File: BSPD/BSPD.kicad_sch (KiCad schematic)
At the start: 82 parts, among them J1 Conn_01x15_Pin, J2 Conn_01x15_Pin, U1 TLV2371DBV, U10 TLV2371DBV, U13 74LVC1G08, U14 AP2204K-ADJ, U15 AP7375Q-50WR-7, U17 74LVC1G08, U18 74LVC1G08, U2 TLV2371DBV, U3 TLV2371DBV, U4 TLV2371DBV, U8 TLV2371DBV, U9 TLV2371DBV

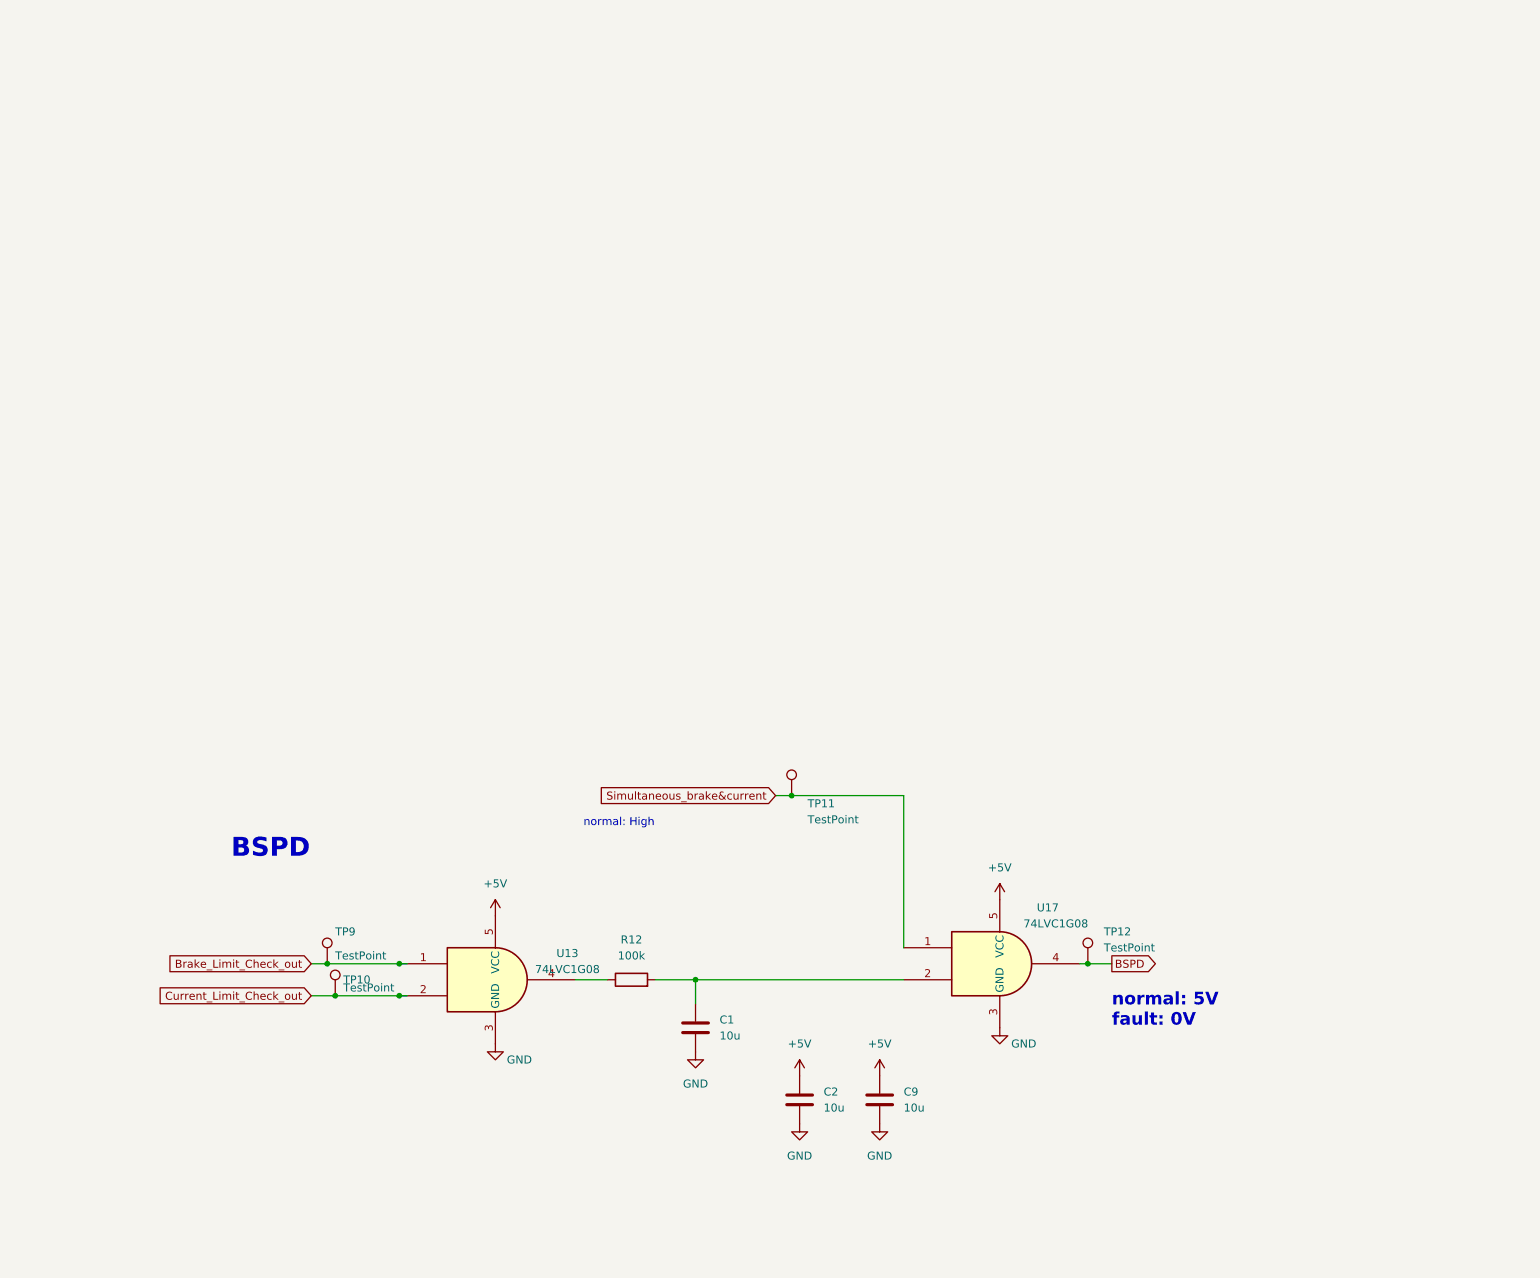
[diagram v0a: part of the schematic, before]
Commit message: BSPD v3 finish basic layout
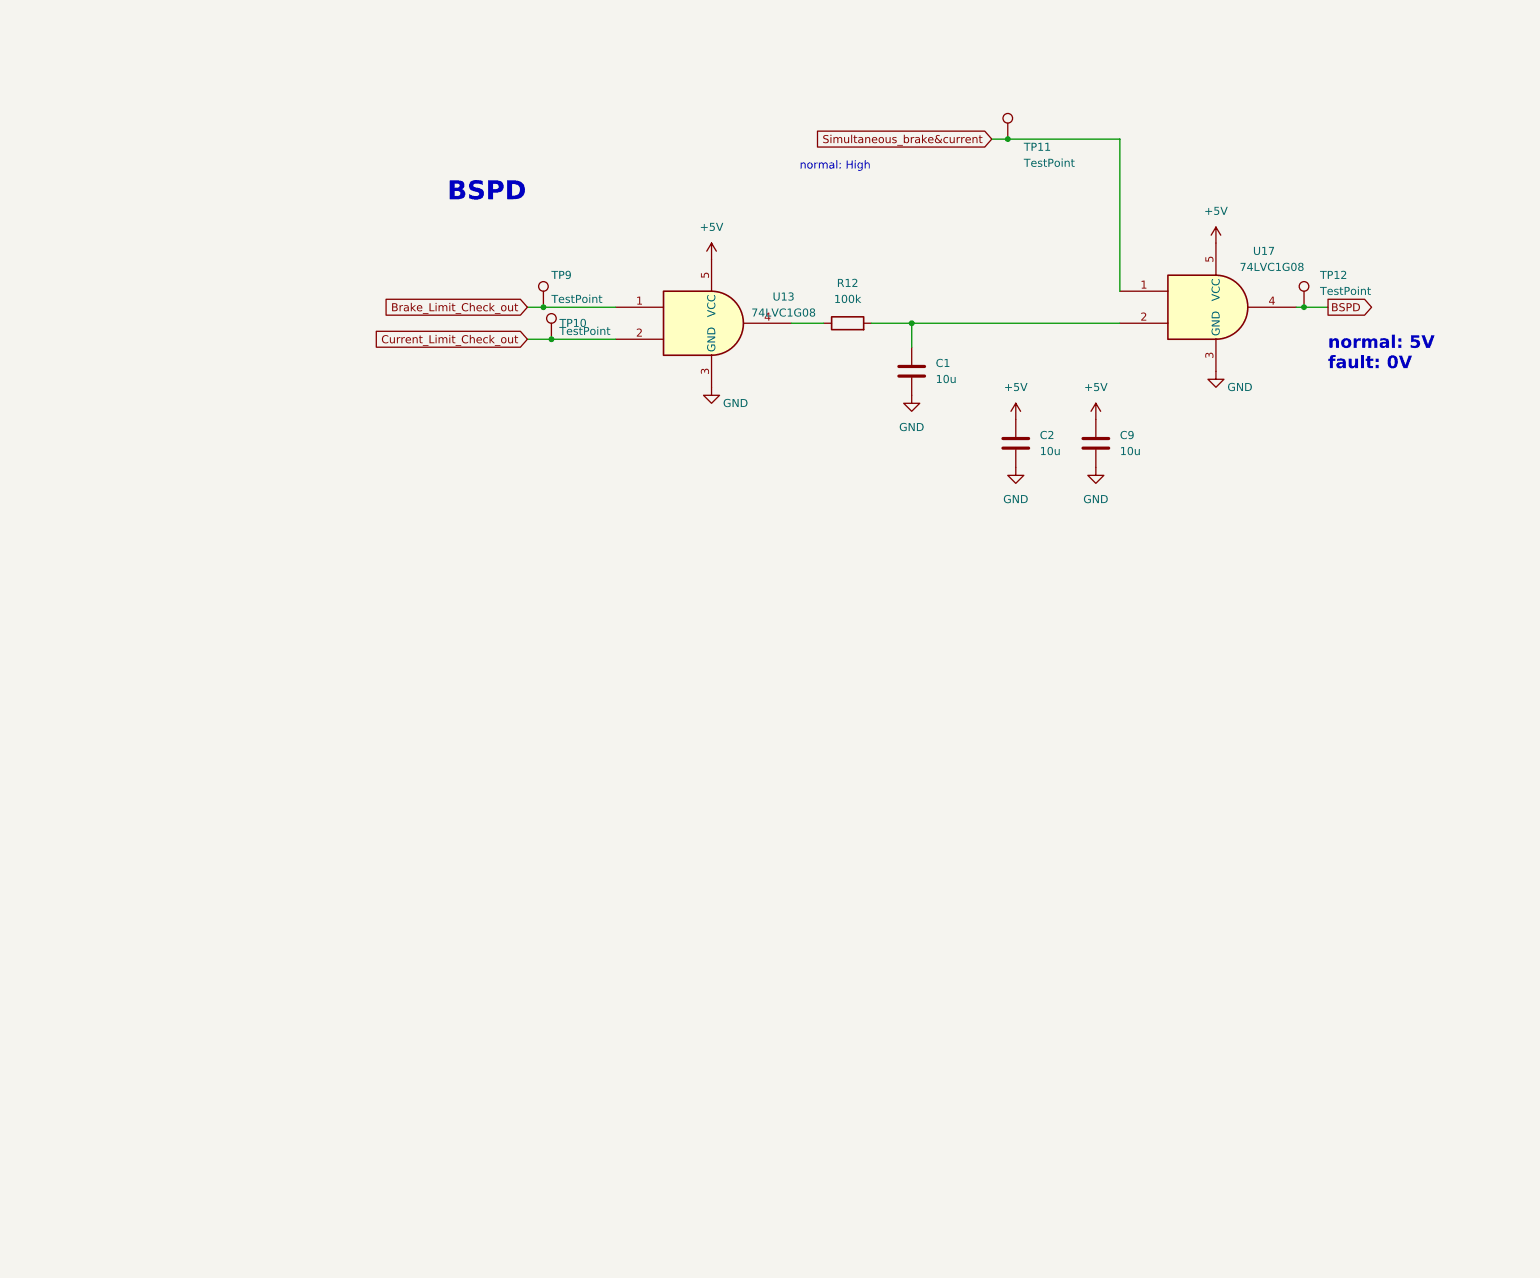
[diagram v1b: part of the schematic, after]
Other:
- moved on the sheet: C1, C2, C9, R12, TP10, TP11, TP12, TP9, U13, U17

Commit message: SDC add pinheader
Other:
- moved on the sheet: C13, C14, C15, C25, C3, C4, C5, D18, D5, D6, D7, R16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

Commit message: Add And gate and R at limit chack
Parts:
- added C6, C7: 10u, Capacitor_SMD:C_0805_2012Metric_Pad1.18x1.45mm_HandSolder, symbol Device:C
- added R11, R13, R7, R9: 10k, Resistor_SMD:R_0603_1608Metric_Pad0.98x0.95mm_HandSolder, symbol Device:R
- added U5, U6: 74LVC1G08, Package_TO_SOT_SMD:SOT-23-5, symbol 74xGxx:74LVC1G08
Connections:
- net +5V: now also C6.1, C7.1, U5.5 (VCC), U6.5 (VCC)
- net Brake_Limit_Check_out: now also U6.4; no longer U3.1, U4.1
- net Current_Limit_Check_out: now also U5.4; no longer U1.1, U2.1
- net GND: now also C6.2, C7.2, U5.3 (GND), U6.3 (GND)
- new net: R7.1, U1.1
- new net: R7.2, U5.1
- new net: R11.1, U3.1
- new net: R11.2, U6.1
- new net: R9.1, U2.1
- new net: R9.2, U5.2
- new net: R13.1, U4.1
- new net: R13.2, U6.2
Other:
- note added: "Throttle Limit Check"
- note removed: "AND 封裝更換 LED 封裝更換 增加TP 6.8->10u"
- note removed: "Current Limit Check"
- title: BSPD_v2 -> BSPD_v3
- moved on the sheet: C13, C14, C15, C25, C3, C4, C5, D1, D18, D2, D5, D6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

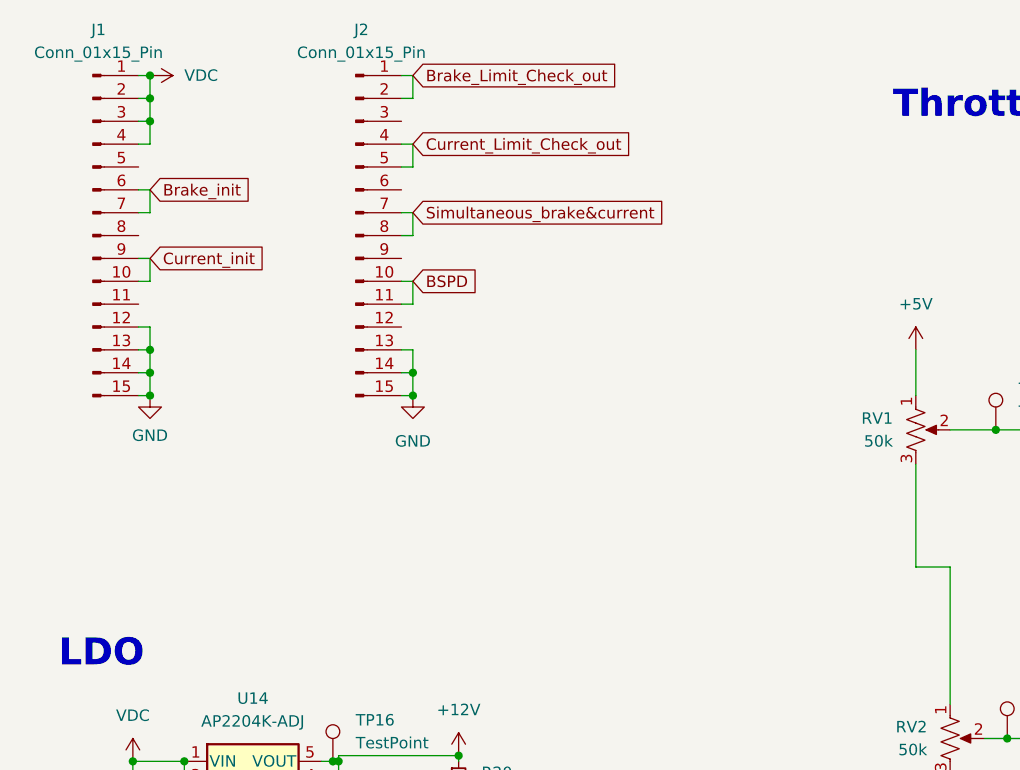
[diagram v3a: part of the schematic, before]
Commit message: BSPD v.3.2 change pin header to 02*10
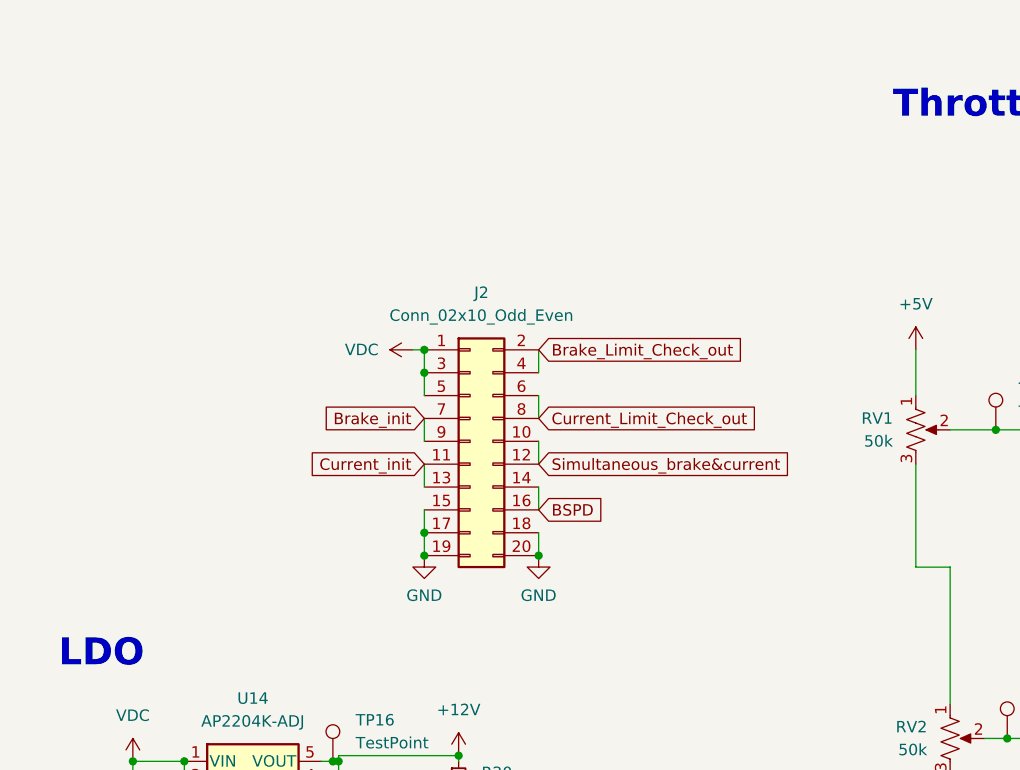
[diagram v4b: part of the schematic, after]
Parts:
- removed J1, J2: Conn_01x15_Pin, Connector_PinHeader_2.54mm:PinHeader_1x15_P2.54mm_Vertical, symbol Connector:Conn_01x15_Pin
- added J2: Conn_02x10_Odd_Even, Connector_PinHeader_2.54mm:PinHeader_2x10_P2.54mm_Vertical, symbol Connector_Generic:Conn_02x10_Odd_Even
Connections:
- net BSPD: now also J2.14 (Pin_14), J2.16 (Pin_16)
- net Brake_Limit_Check_out: now also J2.2 (Pin_2), J2.4 (Pin_4)
- net Brake_init: now also J2.7 (Pin_7), J2.9 (Pin_9)
- net Current_Limit_Check_out: now also J2.6 (Pin_6), J2.8 (Pin_8)
- net Current_init: now also J2.11 (Pin_11), J2.13 (Pin_13)
- net GND: now also J2.15 (Pin_15), J2.17 (Pin_17), J2.18 (Pin_18), J2.19 (Pin_19), J2.20 (Pin_20)
- net Simultaneous_brake&current: now also J2.10 (Pin_10), J2.12 (Pin_12)
- net VDC: now also J2.1 (Pin_1), J2.3 (Pin_3), J2.5 (Pin_5)

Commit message: modify some label
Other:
- title: BSPD_v3 -> BSPD_v3.2
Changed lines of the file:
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@@
   (paper "A2")
   (title_block
-    (title "BSPD_v3")
-    (date "2025-01-30")
+    (title "BSPD_v3.2")
+    (date "2025-03-12")
     (company "Formula Racing")
     (comment 1 "NCKU")

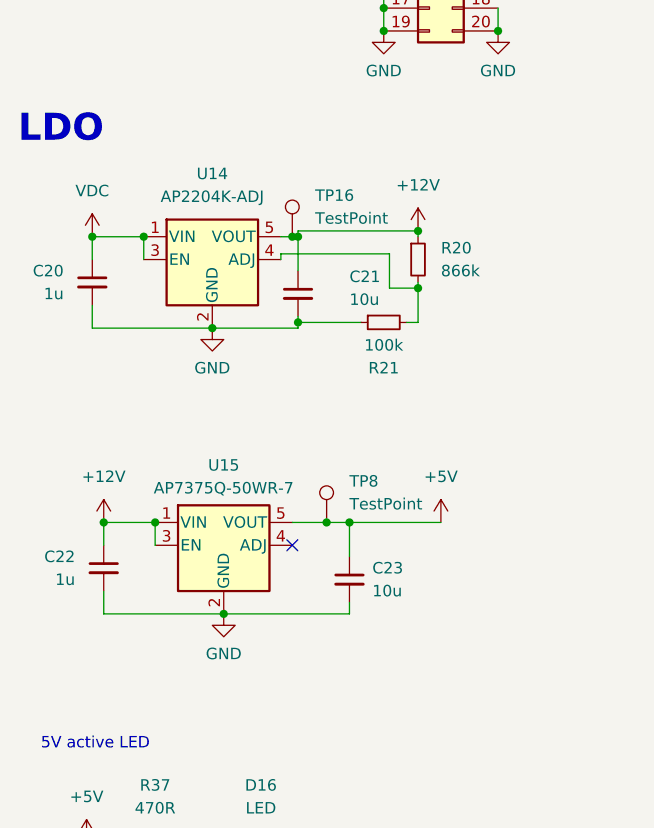
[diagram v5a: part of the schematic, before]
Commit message: remove 12V LDO
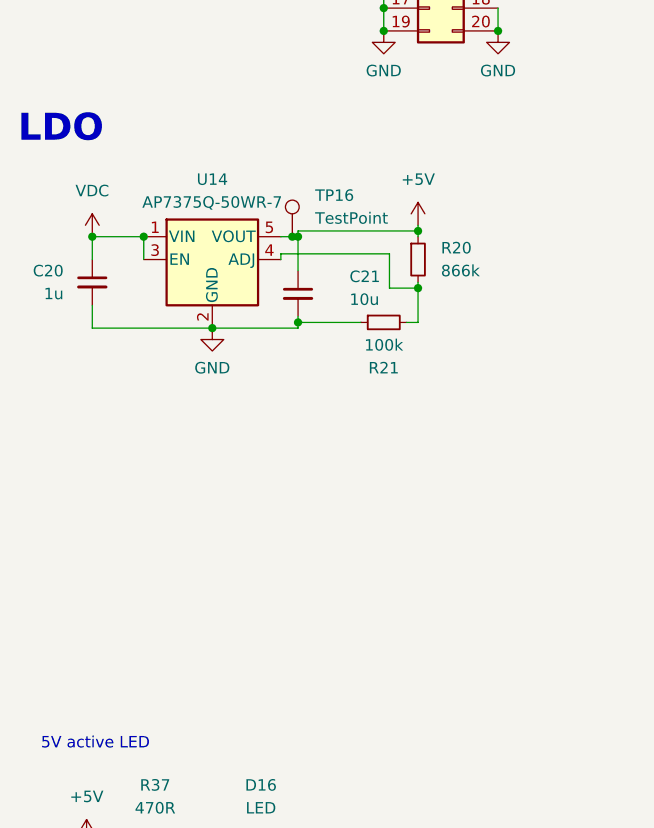
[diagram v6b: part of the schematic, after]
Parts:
- removed C22: 1u, Capacitor_SMD:C_0603_1608Metric_Pad1.08x0.95mm_HandSolder, symbol Device:C_Small
- removed C23: 10u, Capacitor_SMD:C_0805_2012Metric_Pad1.18x1.45mm_HandSolder, symbol Device:C_Small
- removed TP8: TestPoint, TestPoint:TestPoint_THTPad_D2.0mm_Drill1.0mm, symbol Connector:TestPoint
- removed U15: AP7375Q-50WR-7, Package_TO_SOT_SMD:SOT-23-5, symbol Regulator_Linear:AP2204K-ADJ
- U14: value AP2204K-ADJ -> AP7375Q-50WR-7
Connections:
- net +12V is gone; now on net +5V: C21.1, R20.1, TP16.1, U14.5 (VOUT)
- no-connect marks 1 -> 0
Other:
- title: BSPD_v3.2 -> BSPD_v3.3

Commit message: v2025.5
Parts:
- removed C20: 1u, Capacitor_SMD:C_0603_1608Metric_Pad1.08x0.95mm_HandSolder, symbol Device:C_Small
- removed C21: 10u, Capacitor_SMD:C_0805_2012Metric_Pad1.18x1.45mm_HandSolder, symbol Device:C_Small
- removed R20: 866k, Resistor_SMD:R_0603_1608Metric, symbol Device:R_Small
- removed R21: 100k, Resistor_SMD:R_0603_1608Metric, symbol Device:R_Small
- removed R38, R39: 100R, Resistor_SMD:R_0603_1608Metric_Pad0.98x0.95mm_HandSolder, symbol Device:R
- removed U14: AP7375Q-50WR-7, Package_TO_SOT_SMD:SOT-23-5, symbol Regulator_Linear:AP2204K-ADJ
- added C10: 10u, Capacitor_SMD:C_0805_2012Metric, symbol Device:C_Small
- added C11, C20: 0.1u, Capacitor_SMD:C_0603_1608Metric, symbol Device:C
- added C12: 10u, Capacitor_SMD:C_0805_2012Metric, symbol Device:C
- added C8: 1u, Capacitor_SMD:C_0603_1608Metric, symbol Device:C_Small
- added D3, D4: LED, LED_SMD:LED_0805_2012Metric_Pad1.15x1.40mm_HandSolder, symbol Device:LED
- added R14: 866k, Resistor_SMD:R_0603_1608Metric, symbol Device:R_Small
- added R15: 100k, Resistor_SMD:R_0603_1608Metric, symbol Device:R_Small
- added R18, R20, R21, R23, R24: 10k, Resistor_SMD:R_0603_1608Metric, symbol Device:R
- added R19, R29: 1k, Resistor_SMD:R_0603_1608Metric, symbol Device:R
- added R25, R26, R27: 100R, Resistor_SMD:R_0603_1608Metric, symbol Device:R
- added R28: 100R, Resistor_SMD:R_0201_0603Metric, symbol Device:R
- added RV8, RV9: 1M, Potentiometer_THT:Potentiometer_Bourns_3296W_Vertical, symbol Device:R_Potentiometer_US
- added TP15, TP17, TP18, TP8: TestPoint, TestPoint:TestPoint_THTPad_D1.5mm_Drill0.7mm, symbol Connector:TestPoint
- added U11, U14: TLV2371DBV, Package_TO_SOT_SMD:SOT-23-5, symbol Amplifier_Operational:TLV2371DBV
- added U12, U15: 74LVC1G08, Package_TO_SOT_SMD:SOT-23-5, symbol 74xGxx:74LVC1G08
- added U7: AP2204K-ADJ, Package_TO_SOT_SMD:SOT-23-5, symbol Regulator_Linear:AP2204K-ADJ
- C1, C2, C25, C5, C6, C7, C9: footprint Capacitor_SMD:C_0805_2012Metric_Pad1.18x1.45mm_HandSolder -> Capacitor_SMD:C_0805_2012Metric
- C13, C14, C15, C16, C17, C18, C19: value 10u -> 0.1u; footprint Capacitor_SMD:C_0805_2012Metric_Pad1.18x1.45mm_HandSolder -> Capacitor_SMD:C_0603_1608Metric
- C3, C4: footprint Capacitor_SMD:C_0603_1608Metric_Pad1.08x0.95mm_HandSolder -> Capacitor_SMD:C_0603_1608Metric
- R1, R11, R13, R16, R17, R2, R3, R4, R5, R6, R7, R9: footprint Resistor_SMD:R_0603_1608Metric_Pad0.98x0.95mm_HandSolder -> Resistor_SMD:R_0603_1608Metric
- R10, R8: value 470R -> 1k; footprint Resistor_SMD:R_0603_1608Metric_Pad0.98x0.95mm_HandSolder -> Resistor_SMD:R_0603_1608Metric
- R12: value 100k -> 100R; footprint Resistor_SMD:R_0603_1608Metric_Pad0.98x0.95mm_HandSolder -> Resistor_SMD:R_0201_0603Metric
- R22: value 100k -> 50k; footprint Resistor_SMD:R_0603_1608Metric_Pad0.98x0.95mm_HandSolder -> Resistor_SMD:R_0603_1608Metric
- R37: value 470R -> 1k
- RV1, RV2, RV3, RV4, RV5, RV6, RV7: value 50k -> 1M
- TP1, TP10, TP11, TP12, TP13, TP14, TP16, TP2, TP3, TP4, TP5, TP6, TP7, TP9: footprint TestPoint:TestPoint_THTPad_D2.0mm_Drill1.0mm -> TestPoint:TestPoint_THTPad_D1.5mm_Drill0.7mm
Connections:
- net +5V: now also C1.1, C10.1, C11.1, C12.1, C20.1, R14.1, R19.1, R29.1, RV8.1, TP8.1, U11.5 (V+), U12.5 (VCC), U14.5 (V+), U15.5 (VCC), U7.5 (VOUT); no longer TP16.1
- net BSPD: no longer J2.14 (Pin_14)
- net GND: now also C10.2, C11.2, C12.2, C20.2, C8.2, R15.1, RV9.3, U11.2 (V-), U12.3 (GND), U14.2 (V-), U15.3 (GND), U7.2 (GND)
- net VDC: now also C8.1, U7.1 (VIN), U7.3 (EN)
- net current: no longer R2.1, TP13.1
- net at R12.1: now also U15.4; no longer U13.4
- net Brake_Limit_Check_out renamed BSE_L_Fault
- net BSE_L_Fault: now also J2.10 (Pin_10), TP17.1; no longer J2.2 (Pin_2), J2.4 (Pin_4), TP9.1
- net Brake_init renamed BSE_L_init
- net BSE_L_init: now also R25.2; no longer J2.9 (Pin_9)
- net Current_Limit_Check_out renamed APPS_Fault
- net APPS_Fault: now also U15.2; no longer J2.8 (Pin_8), TP10.1, U13.2
- removed net Simultaneous_brake&current: J2.10 (Pin_10), J2.12 (Pin_12), TP11.1, U10.1, U17.1
- net brake renamed BSE_R
- net BSE_R: now also TP10.1, R21.1, R26.1; no longer R5.1, TP14.1
- new net: R24.1, RV9.2, TP16.1
- new net: R20.1, U11.1
- new net: R20.2, U12.1
- new net: R23.2, U12.2
- new net: R12.2, U17.1
- new net: R28.2, U17.2
- new net: R23.1, U14.1
- new net: R21.2, U11.4 (-), U14.3 (+)
- new net: R24.2, U14.4 (-)
- new net: R28.1, U13.4
- new net: R14.2, R15.2, U7.4 (ADJ)
- new net: D3.2 (A), R19.2
- new net: R18.1, RV8.2, TP15.1
- new net: R18.2, U11.3 (+)
- new net: RV8.3, RV9.1
- new net: D4.2 (A), R29.2
- new net APPS: R2.1, R27.1, TP11.1
- new net APPS_init: R27.2
- new net BSE_L: R25.1, R5.1, TP9.1
- new net BSE_R_Fault: D3.1 (K), J2.14 (Pin_14), TP18.1, U12.4, U13.2
- new net BSE_R_init: J2.9 (Pin_9), R26.2
- new net Both: D4.1 (K), J2.2 (Pin_2), U10.1, U15.1
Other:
- title: BSPD_v3.3 -> BSPD_v2025,5
- moved on the sheet: C13, C14, C15, C18, C19, C2, C25, C3, C4, C5, C6, C7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

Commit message: v2025.5
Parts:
- added C21: NC, Capacitor_THT:C_Disc_D3.0mm_W1.6mm_P2.50mm, symbol Device:C_Small
- added R30: 10k, Resistor_SMD:R_0603_1608Metric, symbol Device:R
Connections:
- net APPS is gone; now on net current: R2.1, R27.1, TP11.1
- net APPS_init is gone; now on net current_init: R27.2
- net +5V: now also C21.1
- net APPS_Fault: no longer J2.6 (Pin_6)
- net BSE_L_init: now also J2.19 (Pin_19); no longer J2.7 (Pin_7)
- net BSE_R_Fault: now also C21.2, R30.2; no longer D3.1 (K), U12.4
- net BSE_R_init: now also J2.17 (Pin_17); no longer J2.9 (Pin_9)
- net Both: now also J2.6 (Pin_6); no longer J2.2 (Pin_2)
- net GND: no longer J2.15 (Pin_15), J2.17 (Pin_17), J2.18 (Pin_18), J2.19 (Pin_19), J2.20 (Pin_20)
- net VDC: now also J2.2 (Pin_2); no longer J2.3 (Pin_3), J2.5 (Pin_5)
- net current_init: now reaches J2.8 (Pin_8)
- net current_init: now also J2.20 (Pin_20)
- net Current_init: no longer names the net of J2.11 (Pin_11)
- net Current_init: no longer J2.13 (Pin_13)
- new net: D3.1 (K), R30.1, U12.4
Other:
- moved on the sheet: D1, R8
